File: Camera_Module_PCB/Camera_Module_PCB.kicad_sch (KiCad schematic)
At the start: 4 parts, among them J1 FFC2A32-24-T, J2 DM3AT-SF-PEJM5, SW1 SW_Push, U1 ESP32-S3

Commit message: Updated some elements of the schematic
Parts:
- added D1: Power LED, symbol Device:LED
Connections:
- new net GND: D1.1 (K)
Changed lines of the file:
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@@
 	(generator_version "9.0")
 	(paper "A4")
+	(wire
+		(pts
+			(xy 191.77 24.13) (xy 191.77 26.67)
+		)
+		(stroke
+			(width 0)
+			(type default)
+		)
+	)
+	(wire
+		(pts
+			(xy 191.77 15.24) (xy 191.77 16.51)
+		)
+		(stroke
+			(width 0)
+			(type default)
+		)
+	)
+	(wire
+		(pts
+			(xy 199.39 15.24) (xy 191.77 15.24)
+		)
+		(stroke
+			(width 0)
+			(type default)
+		)
+	)
 	(symbol
 		(lib_id "ESP32-S3:ESP32-S3")
@@
 				(path "/e3d5a9d6-7dc8-43b3-bd64-189ae9cbab33"
 					(reference "U1")
+					(unit 1)
+				)
+			)
+		)
+	)
+	(symbol
+		(lib_id "power:GND")
+		(at 199.39 15.24 90)
+		(unit 1)
+		(exclude_from_sim no)
+		(in_bom yes)
+		(on_board yes)
+		(dnp no)
+		(fields_autoplaced yes)
+		(property "Reference" "#PWR010"
+			(at 205.74 15.24 0)
+			(effects
+				(font
+					(size 1.27 1.27)
+				)
+				(hide yes)
+			)
+		)
+		(property "Value" "GND"
+			(at 203.2 15.2399 90)
+			(effects
+				(font
+					(size 1.27 1.27)
+				)
+				(justify right)
+			)
+		)
+		(property "Footprint" ""
+			(at 199.39 15.24 0)
+			(effects
+				(font
+					(size 1.27 1.27)
+				)
+				(hide yes)
+			)
+		)
+		(property "Datasheet" ""
+			(at 199.39 15.24 0)
+			(effects
+				(font
+					(size 1.27 1.27)
+				)
+				(hide yes)
+			)
+		)
+		(property "Description" "Power symbol creates a global label with name \"GND\" , ground"
+			(at 199.39 15.24 0)
+			(effects
+				(font
+					(size 1.27 1.27)
+				)
+				(hide yes)
+			)
+		)
+		(pin "1"
+		)
+		(instances
+			(project ""
+				(path "/e3d5a9d6-7dc8-43b3-bd64-189ae9cbab33"
+					(reference "#PWR010")
 					(unit 1)
 				)
@@
 					(unit 1)
 				)
+			)
+		)
+	)
+	(symbol
+		(lib_id "Device:LED")
+		(at 191.77 20.32 270)
+		(unit 1)
+		(exclude_from_sim no)
+		(in_bom yes)
+		(on_board yes)
+		(dnp no)
+		(fields_autoplaced yes)
+		(property "Reference" "D1"
+			(at 194.31 17.4624 90)
+			(effects
+				(font
+					(size 1.27 1.27)
+				)
+				(justify left)
+			)
+		)
+		(property "Value" "Power LED"
+			(at 194.31 20.0024 90)
+			(effects
+				(font
+					(size 1.27 1.27)
+				)
+				(justify left)
+			)
+		)
+		(property "Footprint" ""
+			(at 191.77 20.32 0)
+			(effects
+				(font
+					(size 1.27 1.27)
+				)
+				(hide yes)
+			)
+		)
+		(property "Datasheet" "~"
+			(at 191.77 20.32 0)
+			(effects
+				(font
+					(size 1.27 1.27)
+				)
+				(hide yes)
+			)
+		)
+		(property "Description" "Light emitting diode"
+			(at 191.77 20.32 0)
+			(effects
+				(font
+					(size 1.27 1.27)
+				)
+				(hide yes)
+			)
+		)
+		(property "Sim.Pins" "1=K 2=A"
+			(at 191.77 20.32 0)
+			(effects
+				(font
+					(size 1.27 1.27)
+				)
+				(hide yes)
+			)
+		)
+		(pin "1"
+		)
+		(pin "2"
+		)
+		(instances
+			(project ""
+				(path "/e3d5a9d6-7dc8-43b3-bd64-189ae9cbab33"
+					(reference "D1")
+					(unit 1)
+				)

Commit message: Made more small changes to the schematic
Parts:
- added C3, C4, C7, C8: 0.1uF, symbol Device:C_Small
- added C9: 4.7uF, symbol Device:C_Small
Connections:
- net VDDA: now reaches U1.55 (VDDA1)
- net VDDA: now also U1.56 (VDDA2), C3.2, C4.2, C7.2, C8.2, C9.2
- new net +3.3V: C3.1, C4.1, C7.1, C8.1, C9.1
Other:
- note added: "Not sure if VDDA is the supply voltage of the ESP please fact check"

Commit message: Made some small additions and notes
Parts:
- removed J2: DM3AT-SF-PEJM5, DM3AT-SF-PEJM5:HRS_DM3AT-SF-PEJM5, symbol DM3AT-SF-PEJM5 SIM Card:DM3AT-SF-PEJM5
- added R7: 10K, symbol Device:R_US
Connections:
- net GND: now also SW1.2, U1.57 (GND)
- net VDD3P3: now also U1.55 (VDDA1), U1.56 (VDDA2)
- net VDD: now reaches U1.20 (VDD3P3_RTC)
- net VDD: now also C3.2, C4.2, C7.2, C8.2, C9.2, U1.29 (VDD_SPI), U1.46 (VDD3P3_CPU), R7.1
- net at U1.5 (GPIO0): now also SW1.1, R7.2
- removed net VDDA: C3.2, C4.2, C7.2, C8.2, C9.2, U1.55 (VDDA1), U1.56 (VDDA2)
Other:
- note added: "For now these are called VDD and VDDA, but later we might want to change that idk just keep it in mind"
- note added: "This voltage should be clean for VDD application"
- note added: "We should add a reset pin for the MCU as well"
- note added: "When pin 0 is low and the ESP is reset, it enters download mode for USB if I recall properly"
- note removed: "Not sure if VDDA is the supply voltage of the ESP please fact check"
- moved on the sheet: D1, SW1

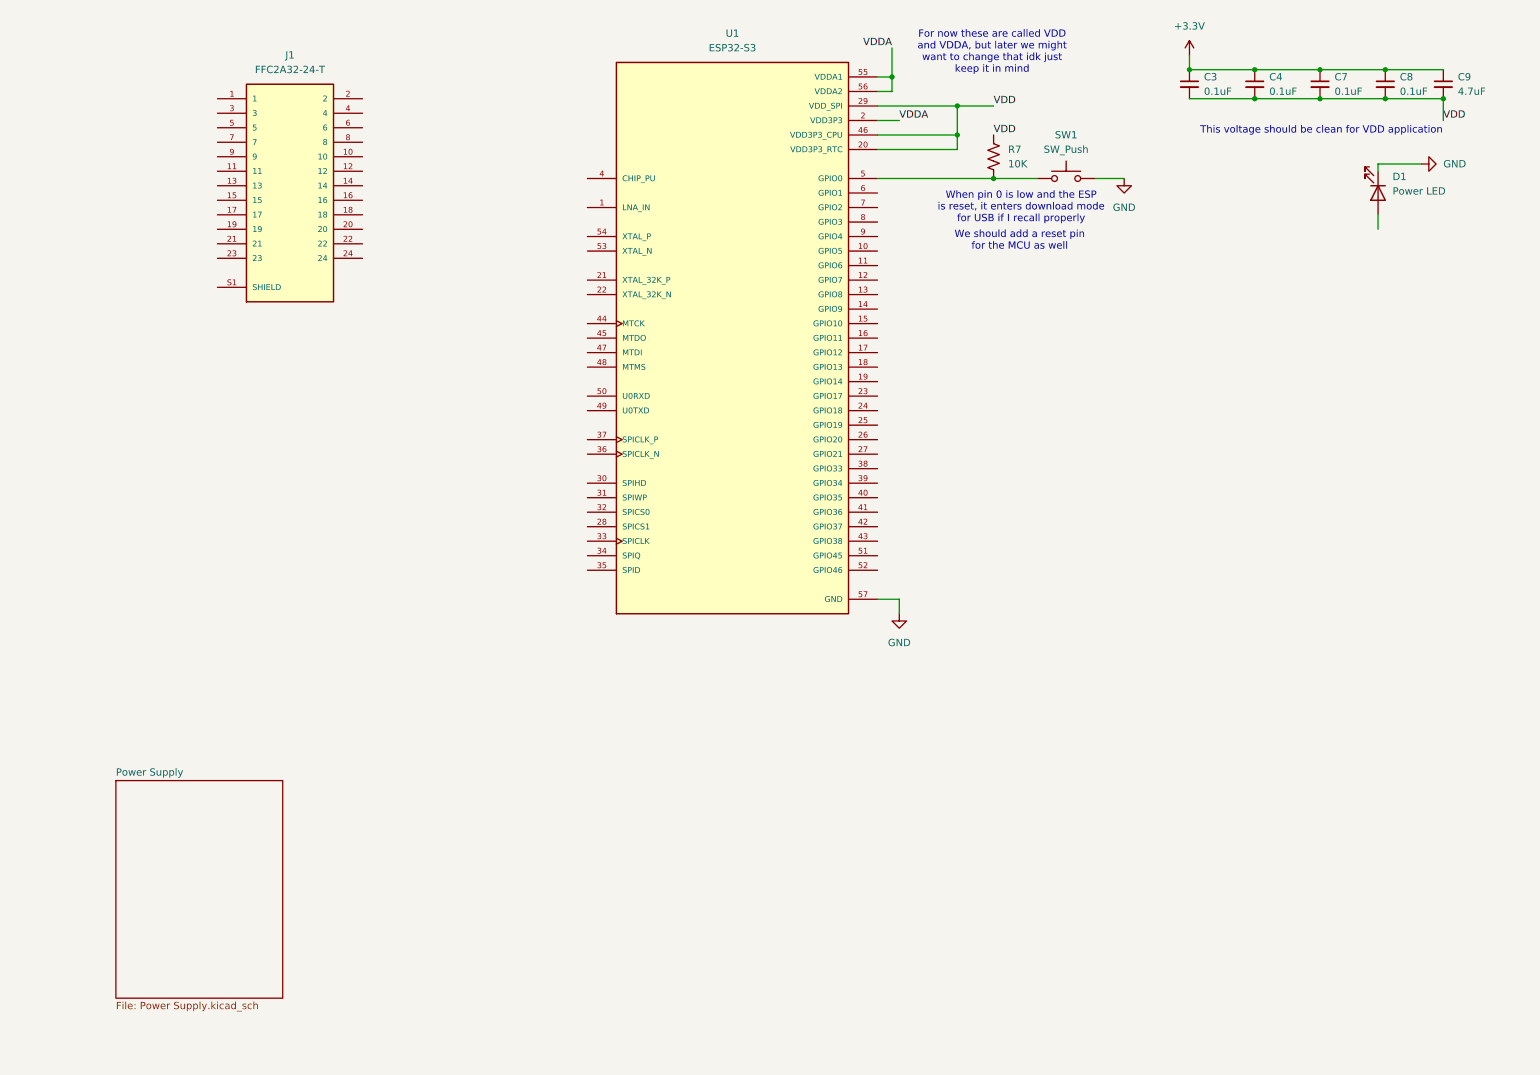
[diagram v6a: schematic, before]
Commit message: Added three new components
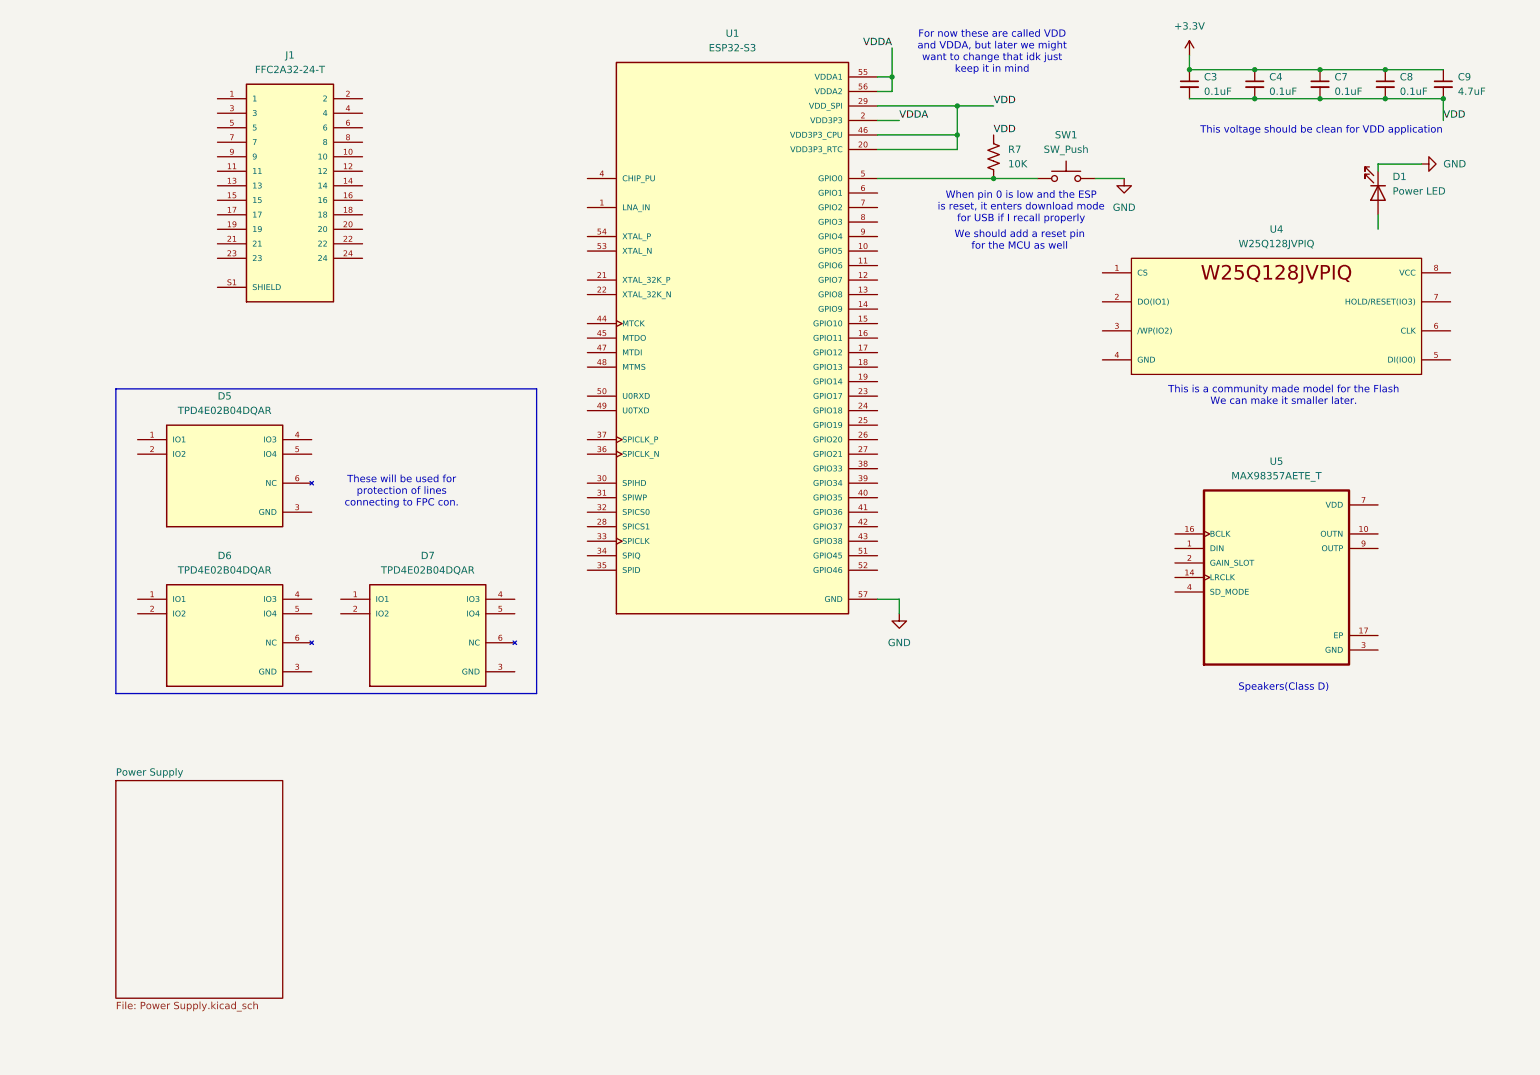
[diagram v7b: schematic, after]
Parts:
- added D5, D6, D7: TPD4E02B04DQAR, TPD4E02B04DQAR:DIO_TPD4E02B04DQAR, symbol TPD4E02B04DQAR (TVS Diodes):TPD4E02B04DQAR
- added U4: W25Q128JVPIQ, W25Q128JVPIQ:W25Q128JVPIQ, symbol W25Q128JVPIQ:W25Q128JVPIQ
- added U5: MAX98357AETE_T, MAX98357AETE_T:QFN50P300X300X80-17N, symbol MAX98357AETE+T:MAX98357AETE_T
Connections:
- net GND: now also D5.3 (GND), D5.8 (GND), D6.3 (GND), D6.8 (GND), D7.3 (GND), D7.8 (GND), U5.11 (GND), U5.15 (GND), U5.3 (GND)
- net VDD: now also U5.7 (VDD), U5.8 (VDD)
- new net: D7.10 (NC), D7.6 (NC), D7.7 (NC), D7.9 (NC)
- new net: D6.10 (NC), D6.6 (NC), D6.7 (NC), D6.9 (NC)
- new net: U4.4 (GND), U4.9 (GND)
- new net: D5.10 (NC), D5.6 (NC), D5.7 (NC), D5.9 (NC)
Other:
- note added: "Speakers(Class D)"
- note added: "These will be used for protection of lines connecting to FPC con."
- note added: "This is a community made model for the Flash We can make it smaller later."

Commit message: Added components and began connections
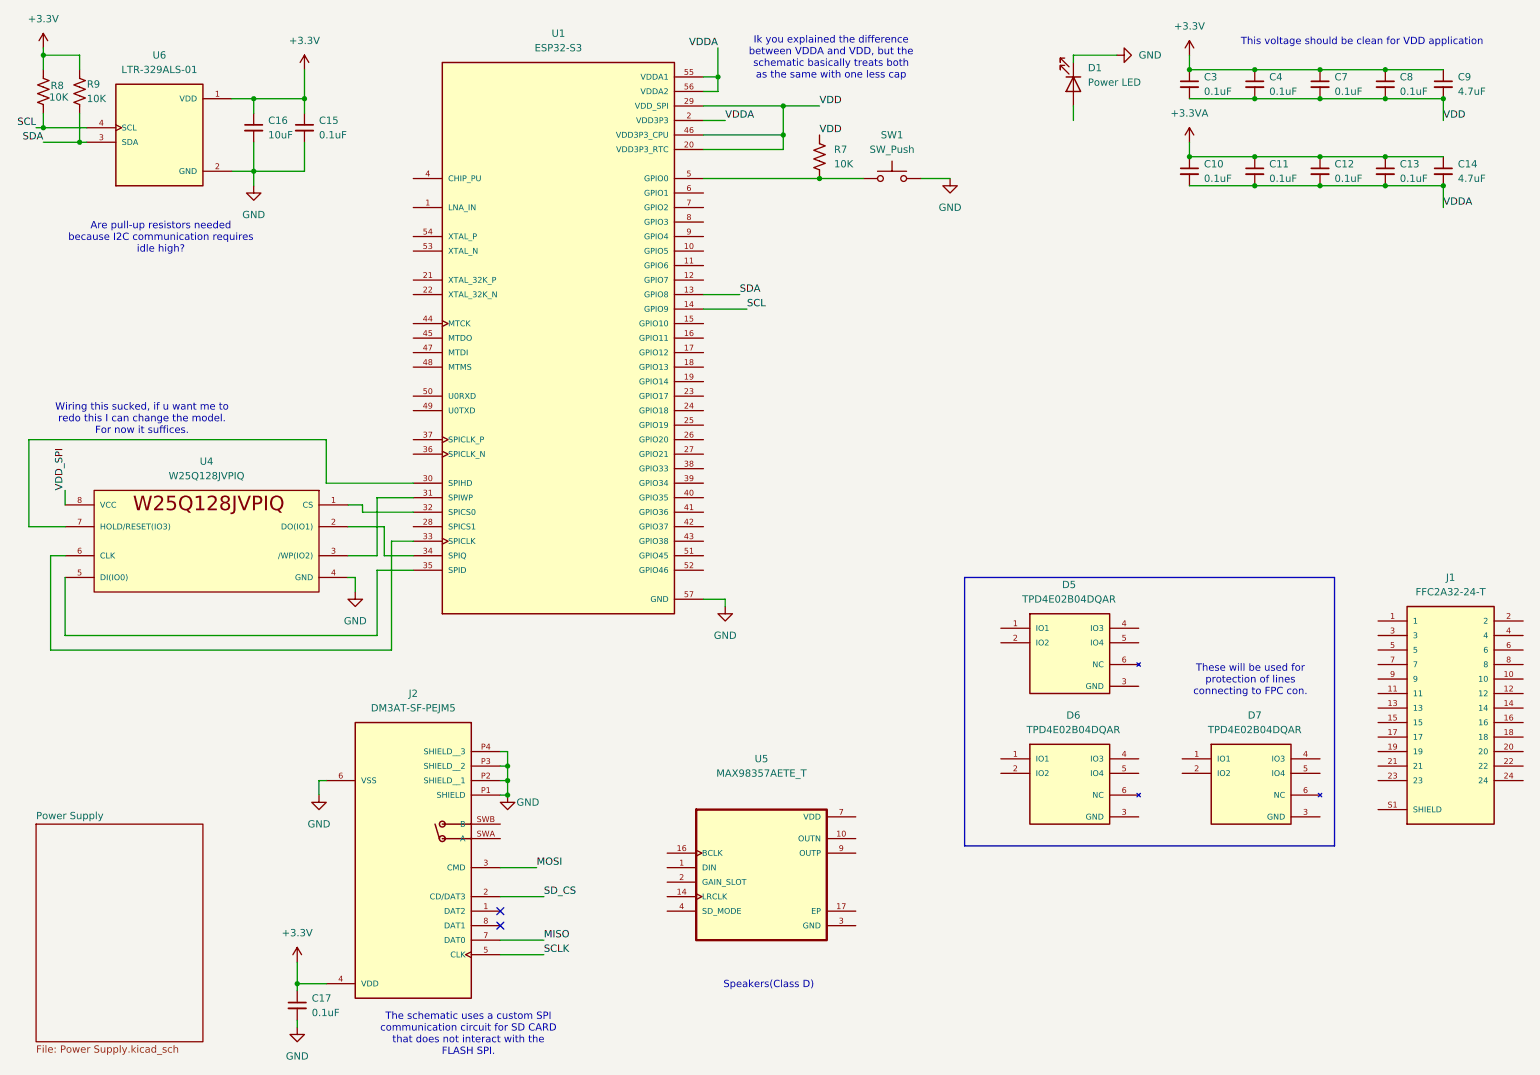
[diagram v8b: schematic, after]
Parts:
- added C10, C11, C12, C13, C15, C17: 0.1uF, symbol Device:C_Small
- added C14: 4.7uF, symbol Device:C_Small
- added C16: 10uF, symbol Device:C_Small
- added J2: DM3AT-SF-PEJM5, DM3AT-SF-PEJM5:HRS_DM3AT-SF-PEJM5, symbol DM3AT-SF-PEJM5 SIM Card:DM3AT-SF-PEJM5
- added R8, R9: 10K, symbol Device:R_US
- added U6: LTR-329ALS-01, LTR-329ALS-01:IC_LTR-329ALS-01, symbol LTR-329ALS-01:LTR-329ALS-01
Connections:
- net +3.3V: now also C15.1, C16.1, C17.1, J2.4 (VDD), R8.1, R9.1, U6.1 (VDD)
- net GND: now also U4.4 (GND), U4.9 (GND), C15.2, C16.2, C17.2, J2.6 (VSS), J2.P1 (SHIELD), J2.P2 (SHIELD__1), J2.P3 (SHIELD__2), J2.P4 (SHIELD__3), U6.2 (GND)
- net VDD3P3: now also C10.2, C11.2, C12.2, C13.2, C14.2
- net SDA: now reaches U1.13 (GPIO8)
- net SDA: now also R9.2, U6.3 (SDA)
- net SCL: now reaches U1.14 (GPIO9)
- net SCL: now also R8.2, U6.4 (SCL)
- net at U1.30 (SPIHD): now also U4.7 (HOLD/RESET(IO3))
- net at U1.31 (SPIWP): now also U4.3 (/WP(IO2))
- net at U1.32 (SPICS0): now also U4.1 (CS)
- net at U1.33 (SPICLK): now also U4.6 (CLK)
- net at U1.34 (SPIQ): now also U4.2 (DO(IO1))
- net at U1.35 (SPID): now also U4.5 (DI(IO0))
- net VDD_SPI: now reaches U4.8 (VCC)
- new net +3.3VA: C10.1, C11.1, C12.1, C13.1, C14.1
- new net MISO: J2.7 (DAT0)
- new net MOSI: J2.3 (CMD)
- new net SCLK: J2.5 (CLK)
- new net SD_CS: J2.2 (CD/DAT3)
- no-connect marks 0 -> 2
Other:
- note added: "Are pull-up resistors needed because I2C communication requires idle high?"
- note added: "Ik you explained the difference between VDDA and VDD, but the schematic basically treats both as the same with one less cap"
- note added: "The schematic uses a custom SPI communication circuit for SD CARD that does not interact with the FLASH SPI."
- note added: "Wiring this sucked, if u want me to redo this I can change the model. For now it suffices."
- note removed: "For now these are called VDD and VDDA, but later we might want to change that idk just keep it in mind"
- note removed: "This is a community made model for the Flash We can make it smaller later."
- note removed: "We should add a reset pin for the MCU as well"
- note removed: "When pin 0 is low and the ESP is reset, it enters download mode for USB if I recall properly"
- moved on the sheet: D1, D5, J1, R7, SW1, U1, U4, U5
